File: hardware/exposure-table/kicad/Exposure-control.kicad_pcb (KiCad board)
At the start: 2 copper layers, 50 x 35 mm, 10 parts, among them J1 Light Control, J2 Power, J3 HDMI, J4 Fan, J5 Safelight Control, J7 UVPanel, Q1 BD139, U1 AMZ_3A_MOD

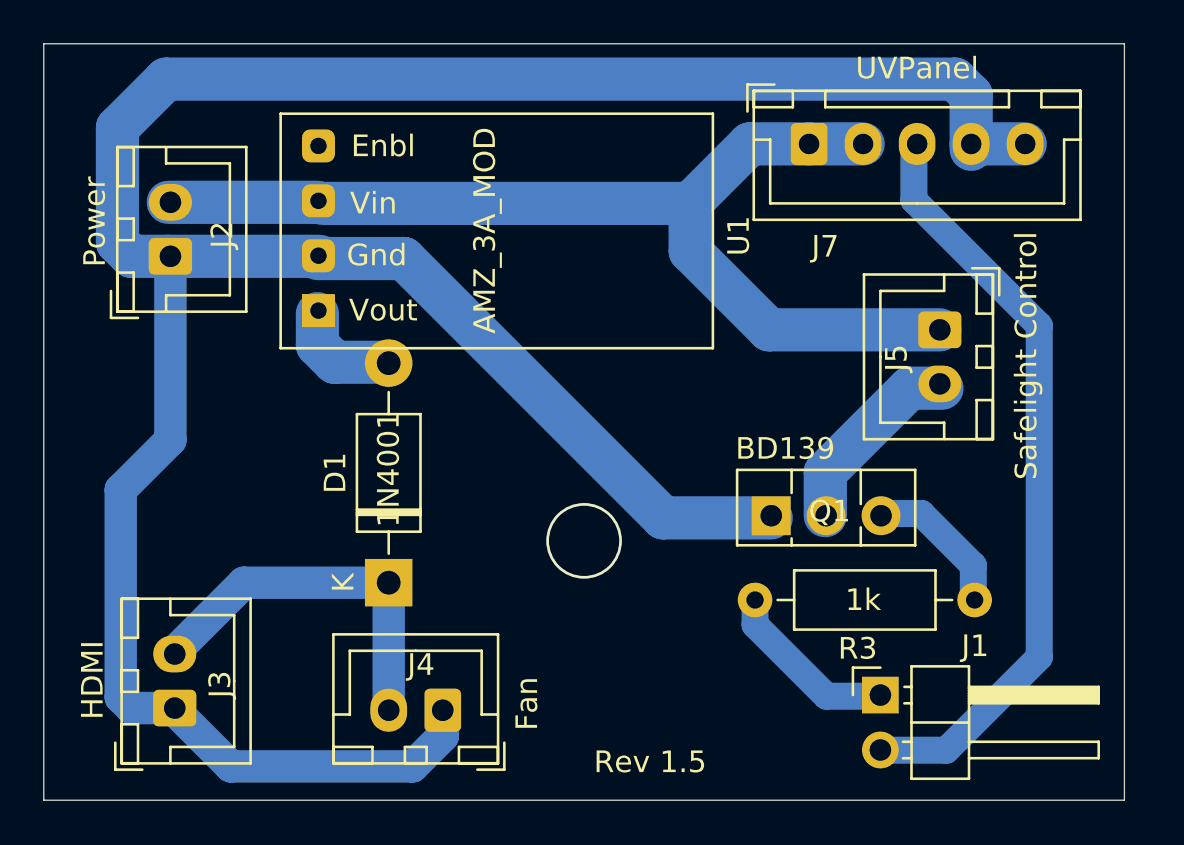
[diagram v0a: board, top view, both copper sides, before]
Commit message: Updated exposure control board
Changed to power MOSFET to control safelight
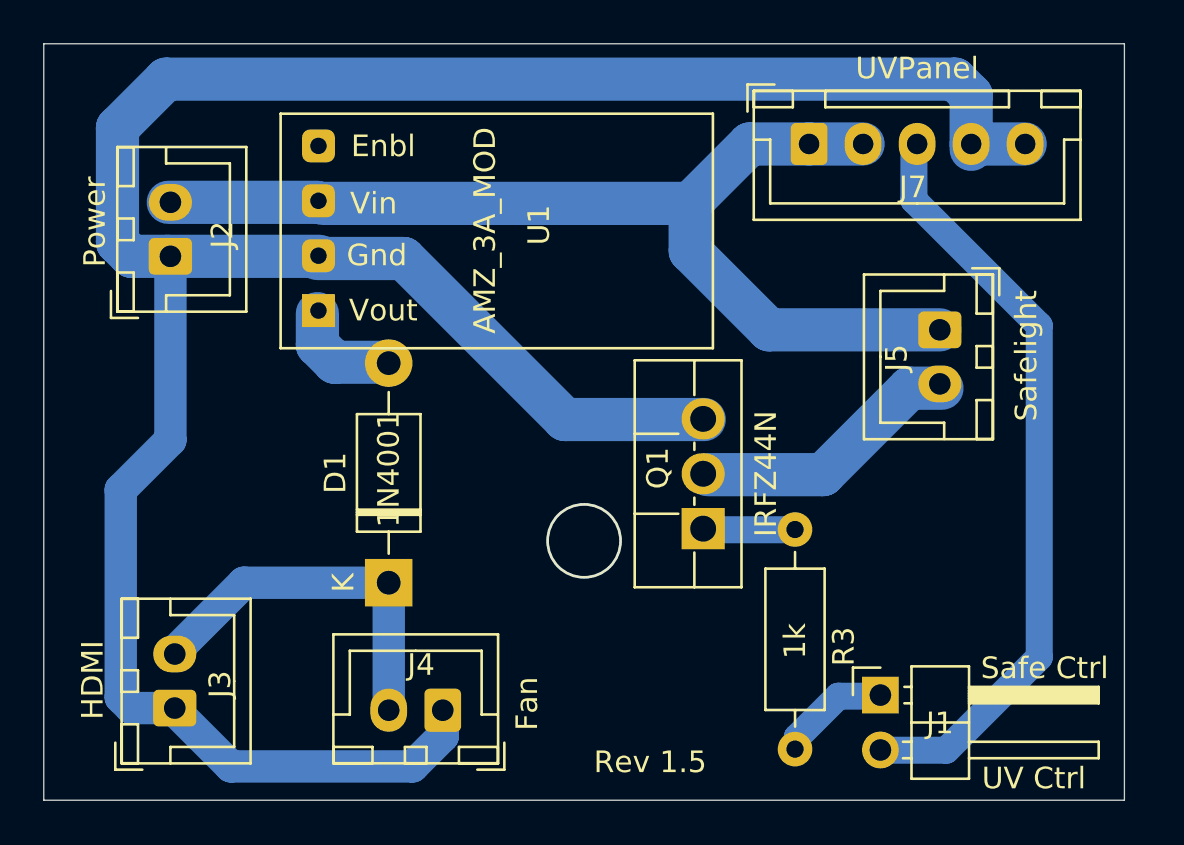
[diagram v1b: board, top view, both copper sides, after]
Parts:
- J5: value Safelight Control -> Safelight
- Q1: value BD139 -> IRFZ44N; footprint Package_TO_SOT_THT:TO-126-3_Vertical -> Package_TO_SOT_THT:TO-220F-3_Vertical
- moved R3 7.14 mm to (44.8, 69.6), turned to 90 degrees
- moved Q1 3.21 mm to (40.5, 59.4), turned to 90 degrees
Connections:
- Q1 pad 1: GND -> Net-(Q1-Pad1)
- Q1 pad 3: Net-(Q1-Pad3) -> GND
- R3 pad 2: Net-(Q1-Pad3) -> Net-(Q1-Pad1)
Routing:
- net Net-(Q1-Pad3): track 6.64 -> 0.00 mm
- net GND: track 126.0 -> 121.1 mm
- net Net-(Q1-Pad1): track 0.00 -> 4.31 mm
- net SafelightGnd: track 9.02 -> 12.5 mm
- net SafelightControl: track 8.17 -> 5.04 mm
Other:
- board text added: "Safe Ctrl"
- board text added: "UV Ctrl"
